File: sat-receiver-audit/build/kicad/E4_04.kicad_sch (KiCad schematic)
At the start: 36 parts, among them Q450 AO3400A, Q451 AO3400A, Q454 AO3400A, Q455 AO3400A, U450 TLV3012BIDBVR, U451 TLV3012BIDBVR, U454 TLV3012BIDBVR, U455 TLV3012BIDBVR

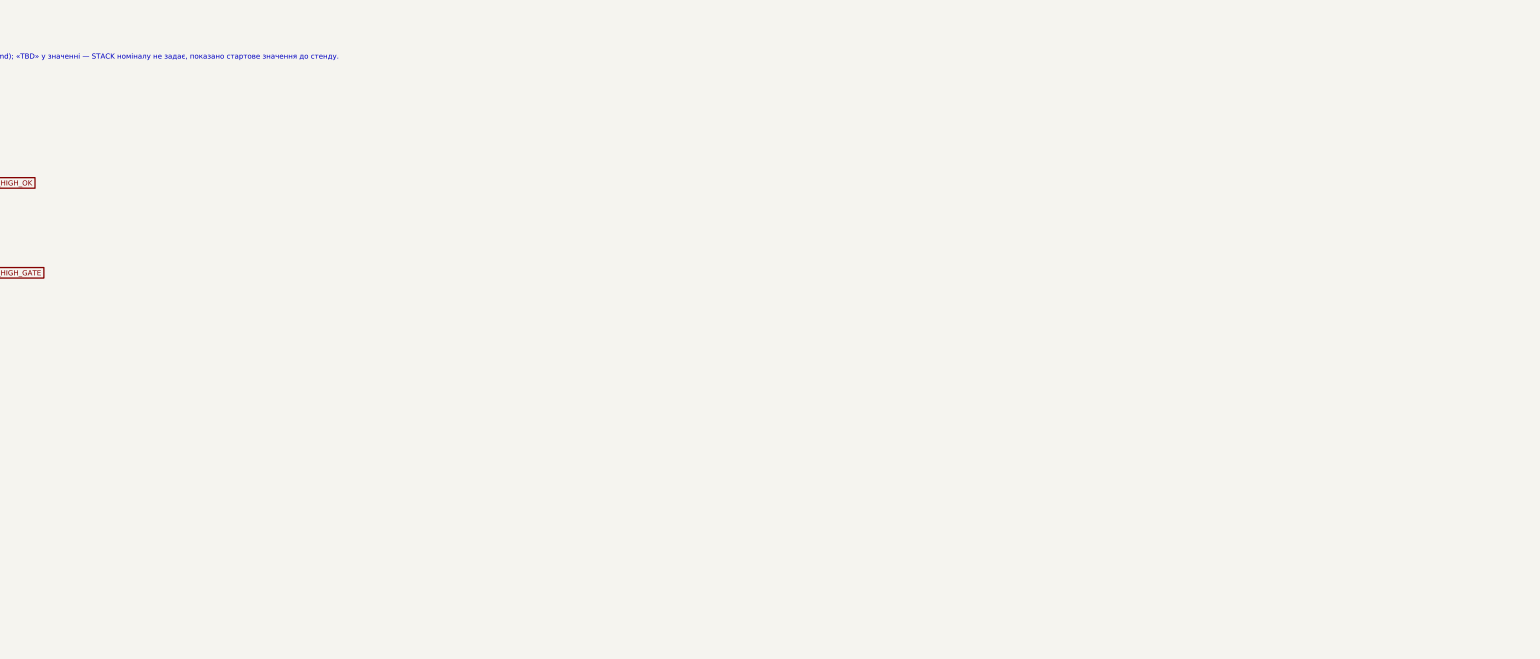
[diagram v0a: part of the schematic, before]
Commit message: Stage 2 integration: CAD and DC_CORE re-freeze from CI run 40094234222; bound-count test and PCB hash lists follow
Co-Authored-By: Claude Opus 5.5 <noreply@anthropic.com>
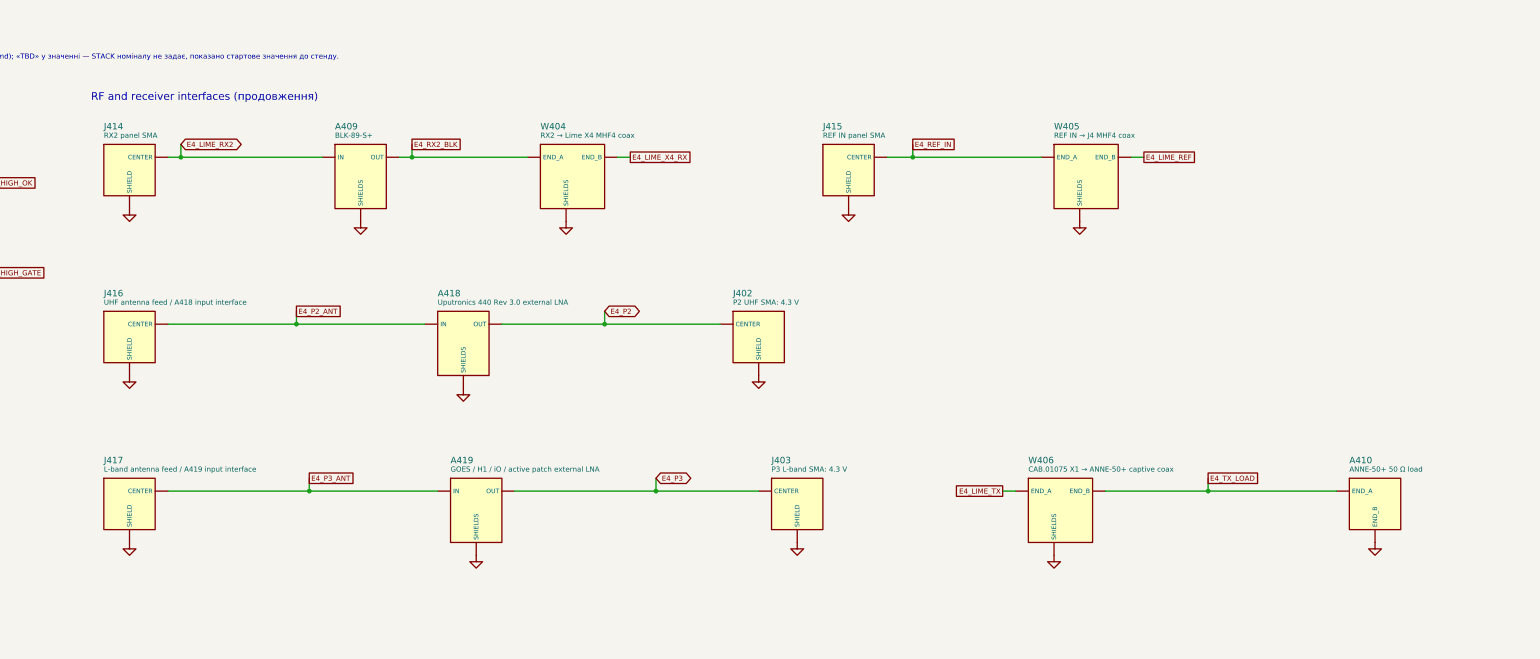
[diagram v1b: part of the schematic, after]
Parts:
- added A409: BLK-89-S+, symbol sr_rx_v2_completed:C_A409
- added A410: ANNE-50+ 50 Ω load, symbol sr_rx_v2_completed:C_A410
- added A418: Uputronics 440 Rev 3.0 external LNA, symbol sr_rx_v2_completed:C_A418
- added A419: GOES / H1 / iO / active patch external LNA, symbol sr_rx_v2_completed:C_A419
- added J402: P2 UHF SMA: 4.3 V, symbol sr_rx_v2_completed:C_J402
- added J403: P3 L-band SMA: 4.3 V, symbol sr_rx_v2_completed:C_J403
- added J414: RX2 panel SMA, symbol sr_rx_v2_completed:C_J414
- added J415: REF IN panel SMA, symbol sr_rx_v2_completed:C_J415
- added J416: UHF antenna feed / A418 input interface, symbol sr_rx_v2_completed:C_J416
- added J417: L-band antenna feed / A419 input interface, symbol sr_rx_v2_completed:C_J417
- added W404: RX2 → Lime X4 MHF4 coax, symbol sr_rx_v2_completed:C_W404
- added W405: REF IN → J4 MHF4 coax, symbol sr_rx_v2_completed:C_W405
- added W406: CAB.01075 X1 → ANNE-50+ captive coax, symbol sr_rx_v2_completed:C_W406
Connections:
- net E4_P2: now also A418.OUT, J402.CENTER
- net GND: now also A409.SHIELDS, A410.END_B, A418.SHIELDS, A419.SHIELDS, J402.SHIELD, J403.SHIELD, J414.SHIELD, J415.SHIELD, J416.SHIELD, J417.SHIELD, W404.SHIELDS, W405.SHIELDS, W406.SHIELDS
- new net E4_LIME_REF: W405.END_B
- new net E4_LIME_RX2: A409.IN, J414.CENTER
- new net E4_LIME_TX: W406.END_A
- new net E4_LIME_X4_RX: W404.END_B
- new net E4_P2_ANT: A418.IN, J416.CENTER
- new net E4_P3: A419.OUT, J403.CENTER
- new net E4_P3_ANT: A419.IN, J417.CENTER
- new net E4_REF_IN: J415.CENTER, W405.END_A
- new net E4_RX2_BLK: A409.OUT, W404.END_A
- new net E4_TX_LOAD: A410.END_A, W406.END_B
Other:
- note added: "RF and receiver interfaces (продовження)"
